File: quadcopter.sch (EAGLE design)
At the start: 67 parts, among them J1 AVR_SPI_PRG_6NS, U1 ATMEGA128RFA1, U2 IMU_LSM9DS1TR, Y1 16MHz

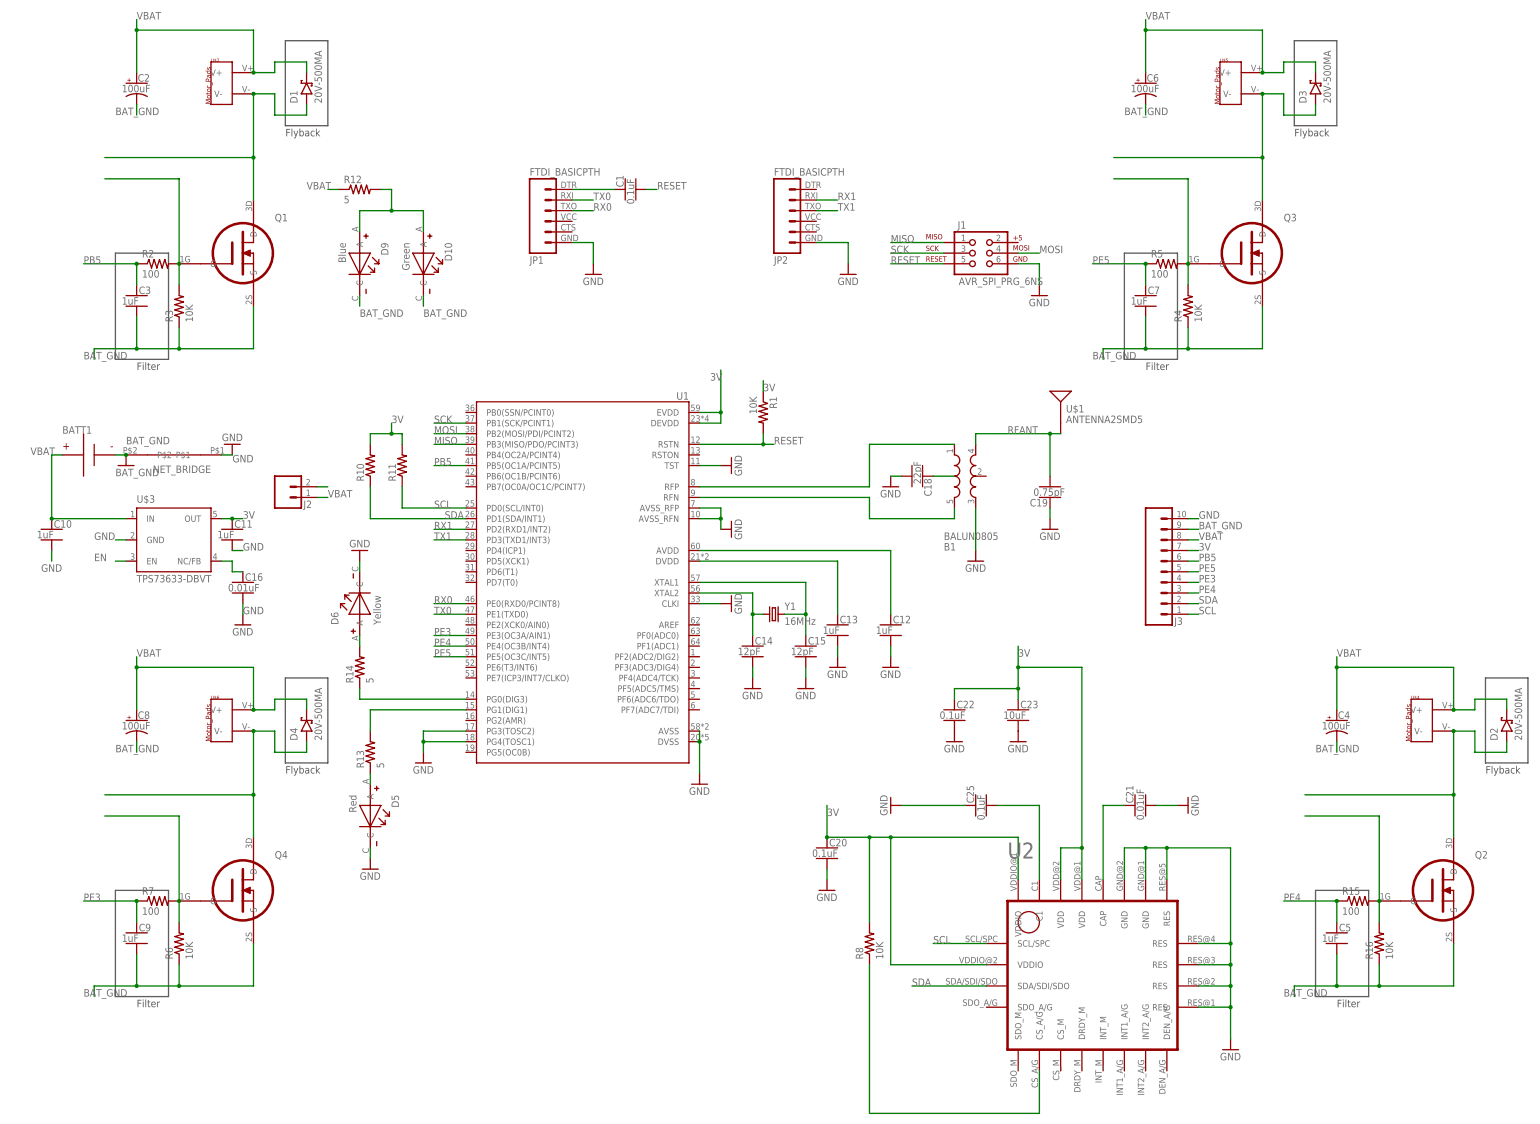
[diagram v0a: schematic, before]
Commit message: Fixed most things from Professor's notes in schematic
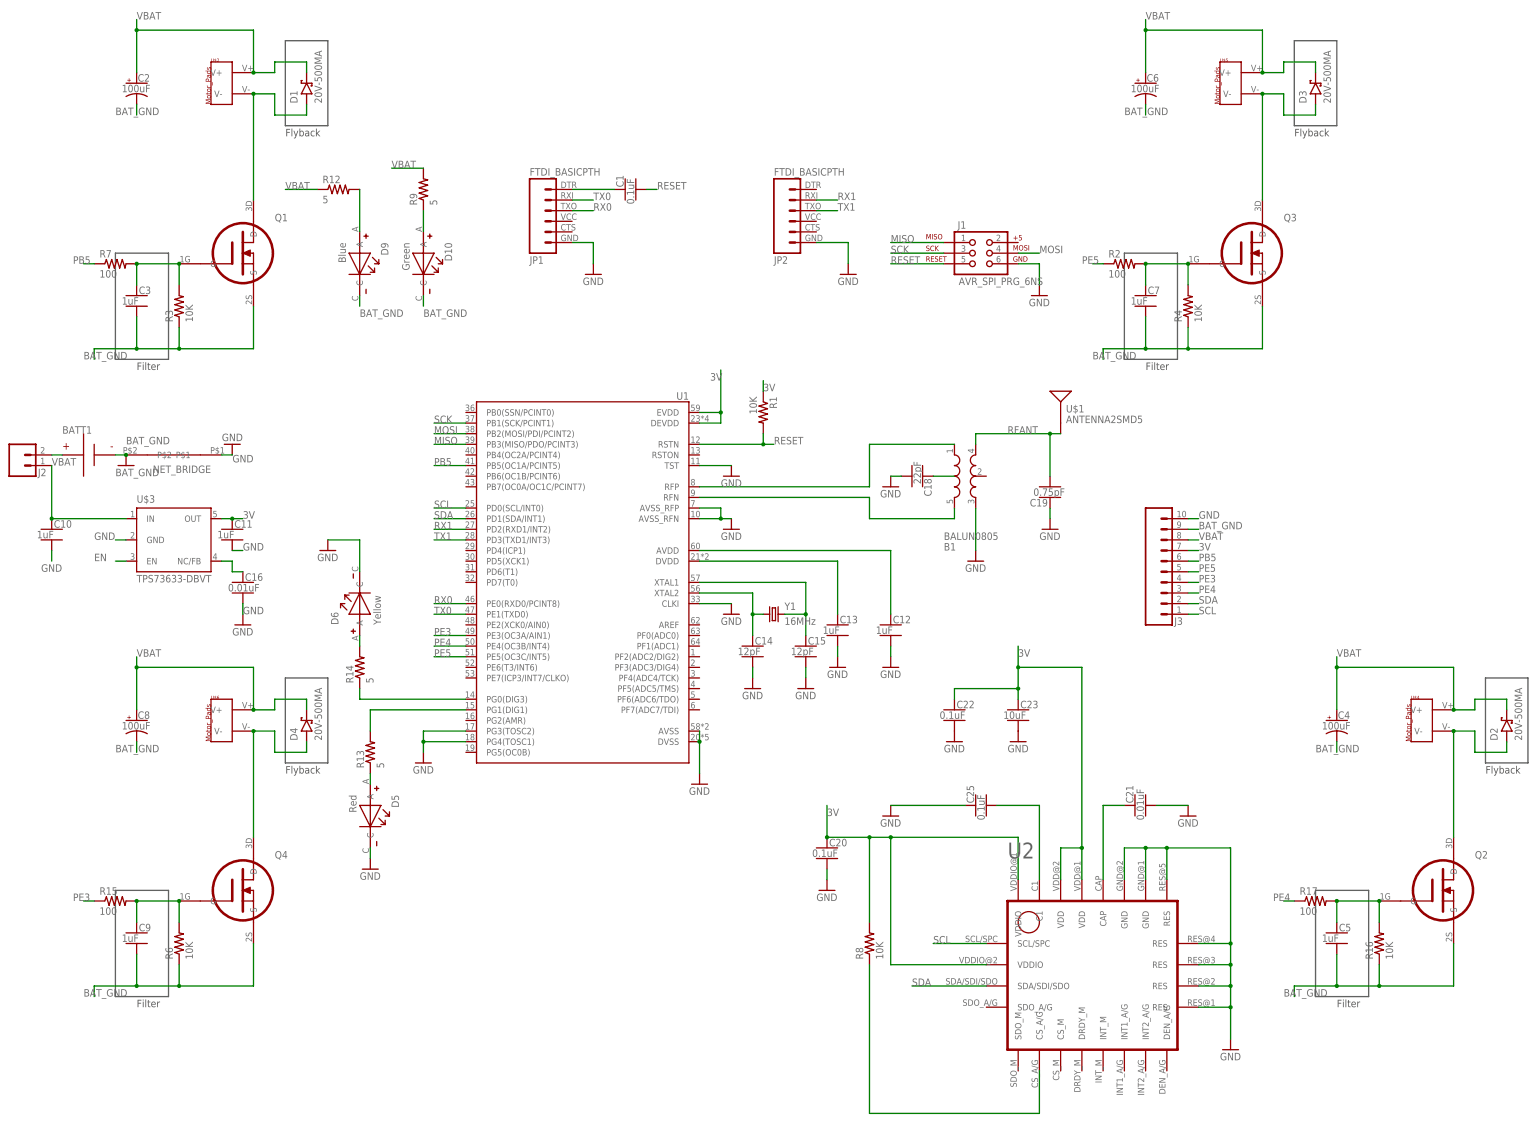
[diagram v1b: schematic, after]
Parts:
- removed R10, R11: (no value), quadparts_prebuilt:RESISTOR_SMD-2012-0805
- removed R5: 100, quadparts_prebuilt:RESISTOR_SMD-2012-0805-100
- added R17: 100, quadparts_prebuilt:RESISTOR_SMD-2012-0805-100
- added R9: 5, quadparts_prebuilt:RESISTOR_SMD-2012-0805
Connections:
- new net N$18: D10.A, R9.1
- new net N$23: BATT1.P, J2.2
- net 3V: no longer R10.2, R11.2
- net FILTERED: now also C7.1, C9.1; no longer Q1.G, Q2.G, R16.2, R3.2, R5.2, R7.2
- net GND: no longer J2.2
- net N$27: no longer D10.A
- net PB5: now also Q1.G, R3.2, R7.1, R7.2; no longer R2.1
- net PE3: now also R15.1; no longer C9.1, R7.1
- net PE4: now also Q2.G, R16.2, R17.1, R17.2; no longer R15.1
- net PE5: now also R2.1; no longer C7.1, R5.1
- net SCL: no longer R11.1
- net SDA: no longer R10.1
- net VBAT: now also R9.2; no longer BATT1.P
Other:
- moved on the sheet: J2, R12, R15, R2, R7

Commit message: stuff
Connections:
- removed net N$16: R8.1, U2.CS_A/G
- net 3V: now also U2.CS_A/G
- net SCL: now also R8.1
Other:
- moved on the sheet: R8
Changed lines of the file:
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@@
 <instance part="C16" gate="G$1" x="-137.16" y="-15.24"/>
 <instance part="GND26" gate="1" x="-137.16" y="-25.4"/>
-<instance part="R8" gate="G$1" x="12.7" y="-101.6" rot="R90"/>
+<instance part="R8" gate="G$1" x="27.94" y="-91.44" rot="R90"/>
 <instance part="R9" gate="G$1" x="-93.98" y="78.74" rot="R90"/>
 <instance part="R17" gate="G$1" x="119.38" y="-91.44"/>
@@
 <pinref part="U2" gate="G$1" pin="VDDIO@1"/>
 <wire x1="48.26" y1="-86.36" x2="48.26" y2="-76.2" width="0.1524" layer="91"/>
-<wire x1="48.26" y1="-76.2" x2="17.78" y2="-76.2" width="0.1524" layer="91"/>
+<wire x1="48.26" y1="-76.2" x2="27.94" y2="-76.2" width="0.1524" layer="91"/>
+<wire x1="27.94" y1="-76.2" x2="17.78" y2="-76.2" width="0.1524" layer="91"/>
 <wire x1="17.78" y1="-76.2" x2="12.7" y2="-76.2" width="0.1524" layer="91"/>
 <wire x1="12.7" y1="-76.2" x2="2.54" y2="-76.2" width="0.1524" layer="91"/>
@@
 <junction x="2.54" y="-76.2"/>
 <pinref part="R8" gate="G$1" pin="2"/>
-<wire x1="12.7" y1="-96.52" x2="12.7" y2="-76.2" width="0.1524" layer="91"/>
+<wire x1="27.94" y1="-86.36" x2="27.94" y2="-76.2" width="0.1524" layer="91"/>
+<junction x="27.94" y="-76.2"/>
+<wire x1="53.34" y1="-142.24" x2="12.7" y2="-142.24" width="0.1524" layer="91"/>
+<pinref part="U2" gate="G$1" pin="CS_A/G"/>
+<wire x1="53.34" y1="-132.08" x2="53.34" y2="-142.24" width="0.1524" layer="91"/>
+<wire x1="12.7" y1="-142.24" x2="12.7" y2="-76.2" width="0.1524" layer="91"/>
 <junction x="12.7" y="-76.2"/>
 </segment>
@@
 <wire x1="40.64" y1="-101.6" x2="27.94" y2="-101.6" width="0.1524" layer="91"/>
 <label x="27.94" y="-101.6" size="1.778" layer="95"/>
+<pinref part="R8" gate="G$1" pin="1"/>
+<wire x1="27.94" y1="-101.6" x2="27.94" y2="-96.52" width="0.1524" layer="91"/>
 </segment>
 </net>
@@
 </segment>
 </net>
-<net name="N$16" class="0">
-<segment>
-<wire x1="53.34" y1="-142.24" x2="12.7" y2="-142.24" width="0.1524" layer="91"/>
-<pinref part="U2" gate="G$1" pin="CS_A/G"/>
-<wire x1="53.34" y1="-132.08" x2="53.34" y2="-142.24" width="0.1524" layer="91"/>
-<pinref part="R8" gate="G$1" pin="1"/>
-<wire x1="12.7" y1="-106.68" x2="12.7" y2="-142.24" width="0.1524" layer="91"/>
-</segment>
-</net>

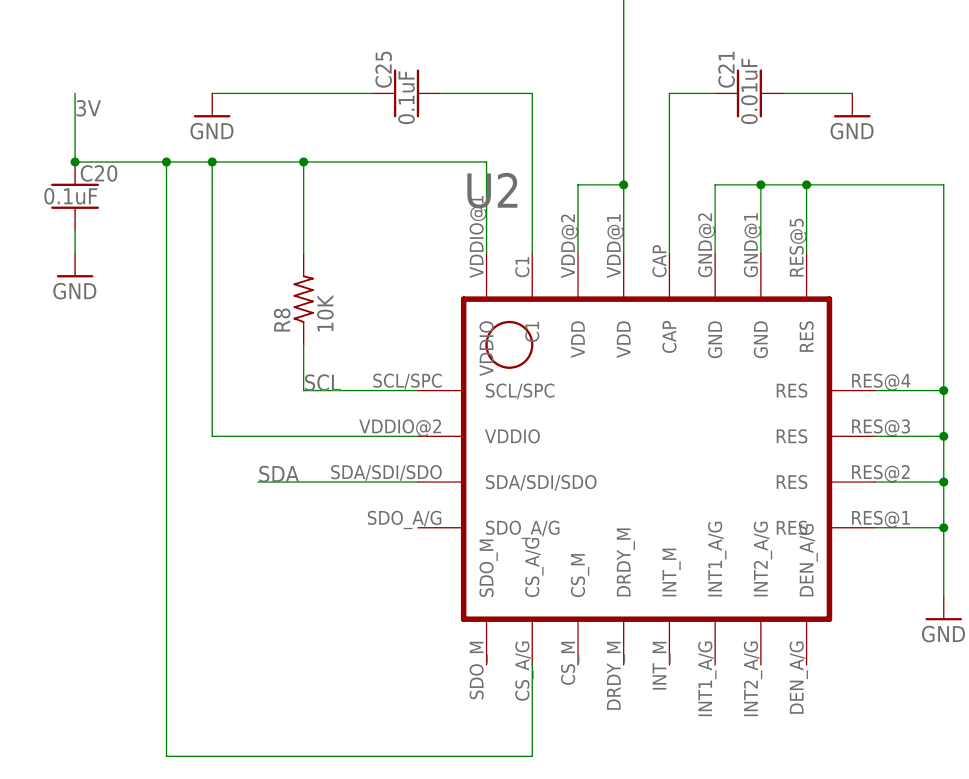
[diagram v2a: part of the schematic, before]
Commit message: IMU is correct now I think?
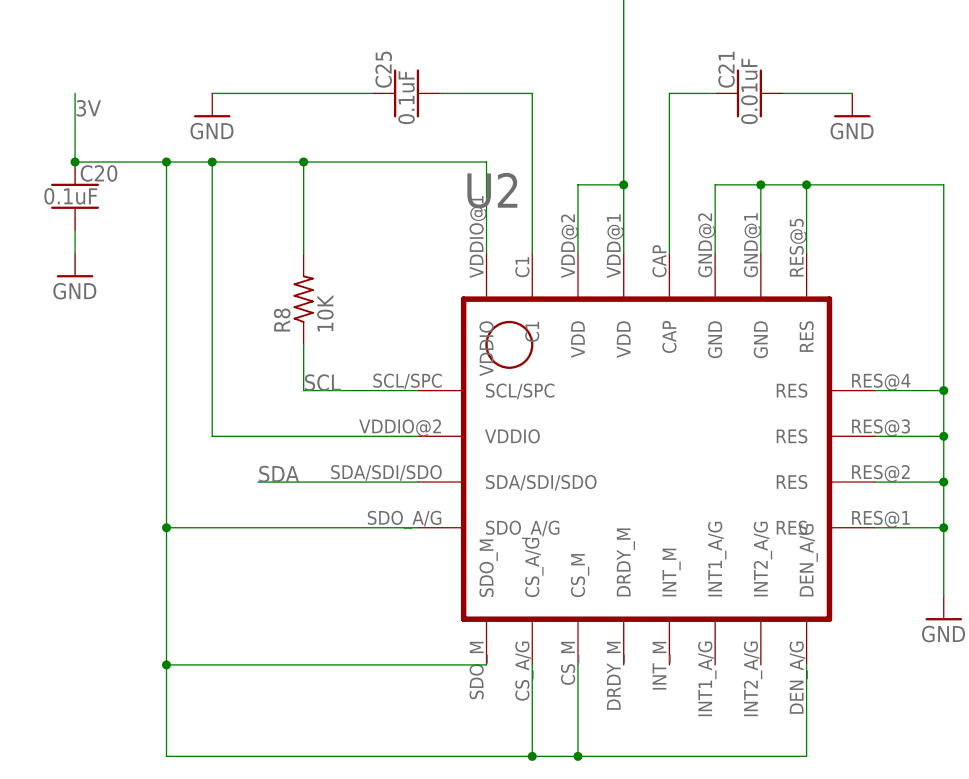
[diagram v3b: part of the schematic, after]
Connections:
- net 3V: now also U2.CS_M, U2.DEN_A/G, U2.SDO_A/G, U2.SDO_M
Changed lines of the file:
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@@
 <pinref part="U2" gate="G$1" pin="CS_A/G"/>
 <wire x1="53.34" y1="-132.08" x2="53.34" y2="-142.24" width="0.1524" layer="91"/>
-<wire x1="12.7" y1="-142.24" x2="12.7" y2="-76.2" width="0.1524" layer="91"/>
+<wire x1="12.7" y1="-142.24" x2="12.7" y2="-132.08" width="0.1524" layer="91"/>
 <junction x="12.7" y="-76.2"/>
+<pinref part="U2" gate="G$1" pin="SDO_A/G"/>
+<wire x1="12.7" y1="-132.08" x2="12.7" y2="-116.84" width="0.1524" layer="91"/>
+<wire x1="12.7" y1="-116.84" x2="12.7" y2="-76.2" width="0.1524" layer="91"/>
+<wire x1="40.64" y1="-116.84" x2="12.7" y2="-116.84" width="0.1524" layer="91"/>
+<junction x="12.7" y="-116.84"/>
+<pinref part="U2" gate="G$1" pin="CS_M"/>
+<wire x1="58.42" y1="-132.08" x2="58.42" y2="-142.24" width="0.1524" layer="91"/>
+<wire x1="58.42" y1="-142.24" x2="53.34" y2="-142.24" width="0.1524" layer="91"/>
+<junction x="53.34" y="-142.24"/>
+<pinref part="U2" gate="G$1" pin="SDO_M"/>
+<wire x1="48.26" y1="-132.08" x2="12.7" y2="-132.08" width="0.1524" layer="91"/>
+<junction x="12.7" y="-132.08"/>
+<pinref part="U2" gate="G$1" pin="DEN_A/G"/>
+<wire x1="83.82" y1="-132.08" x2="83.82" y2="-142.24" width="0.1524" layer="91"/>
+<wire x1="83.82" y1="-142.24" x2="58.42" y2="-142.24" width="0.1524" layer="91"/>
+<junction x="58.42" y="-142.24"/>
 </segment>
 <segment>

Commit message: fixed some schematic stuff
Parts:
- removed R12, R13, R14: 5, quadparts_prebuilt:RESISTOR_SMD-2012-0805
- added R10, R11, R5: 100, quadparts_prebuilt:RESISTOR_SMD-2012-0805-100
- Q1, Q2, Q3, Q4: value (none) -> 2.6A
- R9: value 5 -> 100; device quadparts_prebuilt:RESISTOR_SMD-2012-0805 -> quadparts_prebuilt:RESISTOR_SMD-2012-0805-100
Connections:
- removed net EN: U$3.EN
- removed net FLYBACK: D1.A, D2.A, D3.A, D4.A, Q1.D, Q2.D, Q3.D, Q4.D, U$2.V-, U$4.V-, U$5.V-, U$6.V-
- new net N$16: D1.A, Q1.D, U$2.V-
- new net N$24: D3.A, Q3.D, U$5.V-
- new net N$29: D4.A, Q4.D, U$6.V-
- new net N$30: D2.A, Q2.D, U$4.V-
- new net N$31: C7.1, Q3.G, R2.2, R4.2
- new net N$32: C16.1, U$3.NC/FB
- new net N$33: C3.1, Q1.G, R3.2, R7.2
- new net N$34: C5.1, Q2.G, R16.2, R17.2
- net FILTERED: no longer C7.1, Q3.G, R2.2, R4.2
- net GND: no longer C16.1, U$3.NC/FB
- net N$18: now also R10.2; no longer R9.1
- net N$19: now also R9.2; no longer R13.1
- net N$20: now also R5.2; no longer R14.1
- net N$26: now also R9.1; no longer R13.2
- net N$27: now also R11.1; no longer R12.2
- net N$28: now also R5.1; no longer R14.2
- net PB5: no longer C3.1, Q1.G, R3.2, R7.2
- net PE4: no longer C5.1, Q2.G, R16.2, R17.2
- net VBAT: now also R10.1, R11.2; no longer R12.1, R9.2
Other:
- moved on the sheet: R9

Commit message: Some changes to brd
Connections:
- net GND: now also B1.GND@5; no longer B1.OUT2
- net N$21: now also B1.OUT1; no longer B1.IN
- net N$22: now also B1.OUT2; no longer B1.GND@5
- net N$25: now also B1.GND@2
- net RFANT: now also B1.IN; no longer B1.OUT1
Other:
- moved on the sheet: B1, U$1
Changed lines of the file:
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@@
 <?xml version="1.0" encoding="utf-8"?>
 <!DOCTYPE eagle SYSTEM "eagle.dtd">
-<eagle version="8.1.1">
+<eagle version="8.0.0">
 <drawing>
 <settings>
@@
 <instance part="JP2" gate="G$1" x="-5.08" y="73.66" rot="MR180"/>
 <instance part="J1" gate="G$1" x="38.1" y="63.5"/>
-<instance part="U$1" gate="G$1" x="58.42" y="25.4"/>
+<instance part="U$1" gate="G$1" x="55.88" y="25.4"/>
 <instance part="GND1" gate="1" x="-53.34" y="58.42"/>
 <instance part="C1" gate="G$1" x="-45.72" y="78.74" rot="R90"/>
@@
 <instance part="GND13" gate="1" x="-93.98" y="-58.42"/>
 <instance part="GND14" gate="1" x="-27.94" y="-63.5"/>
-<instance part="B1" gate="G$1" x="35.56" y="12.7"/>
+<instance part="B1" gate="G$1" x="35.56" y="12.7" rot="MR0"/>
 <instance part="C18" gate="G$1" x="25.4" y="10.16" rot="R270"/>
 <instance part="GND15" gate="1" x="17.78" y="7.62"/>
@@
 </segment>
 <segment>
-<pinref part="B1" gate="G$1" pin="OUT2"/>
-<pinref part="GND16" gate="1" pin="GND"/>
-<wire x1="38.1" y1="2.54" x2="38.1" y2="-7.62" width="0.1524" layer="91"/>
-</segment>
-<segment>
 <pinref part="C19" gate="G$1" pin="1"/>
 <wire x1="55.88" y1="2.54" x2="55.88" y2="0" width="0.1524" layer="91"/>
@@
 <wire x1="-116.84" y1="-5.08" x2="-109.22" y2="-5.08" width="0.1524" layer="91"/>
 <wire x1="-109.22" y1="-5.08" x2="-109.22" y2="-12.7" width="0.1524" layer="91"/>
+</segment>
+<segment>
+<pinref part="B1" gate="G$1" pin="GND@5"/>
+<pinref part="GND16" gate="1" pin="GND"/>
+<wire x1="38.1" y1="2.54" x2="38.1" y2="-7.62" width="0.1524" layer="91"/>
 </segment>
 </net>
@@
 <wire x1="-27.94" y1="7.62" x2="12.7" y2="7.62" width="0.1524" layer="91"/>
 <wire x1="12.7" y1="7.62" x2="12.7" y2="17.78" width="0.1524" layer="91"/>
-<pinref part="B1" gate="G$1" pin="IN"/>
+<pinref part="B1" gate="G$1" pin="OUT1"/>
 <wire x1="12.7" y1="17.78" x2="33.02" y2="17.78" width="0.1524" layer="91"/>
 </segment>
@@
 <wire x1="-27.94" y1="5.08" x2="12.7" y2="5.08" width="0.1524" layer="91"/>
 <wire x1="12.7" y1="5.08" x2="12.7" y2="0" width="0.1524" layer="91"/>
-<pinref part="B1" gate="G$1" pin="GND@5"/>
-<wire x1="33.02" y1="0" x2="33.02" y2="2.54" width="0.1524" layer="91"/>
 <wire x1="12.7" y1="0" x2="33.02" y2="0" width="0.1524" layer="91"/>
-</segment>
-</net>
-<net name="N$25" class="0">
-<segment>
-<wire x1="33.02" y1="10.16" x2="27.94" y2="10.16" width="0.1524" layer="91"/>
-<pinref part="C18" gate="G$1" pin="1"/>
+<pinref part="B1" gate="G$1" pin="OUT2"/>
+<wire x1="33.02" y1="2.54" x2="33.02" y2="0" width="0.1524" layer="91"/>
 </segment>
 </net>
 <net name="RFANT" class="1">
 <segment>
-<pinref part="B1" gate="G$1" pin="OUT1"/>
-<wire x1="38.1" y1="17.78" x2="38.1" y2="20.32" width="0.1524" layer="91"/>
-<wire x1="38.1" y1="20.32" x2="55.88" y2="20.32" width="0.1524" layer="91"/>
 <pinref part="U$1" gate="G$1" pin="SIGNAL"/>
-<wire x1="55.88" y1="20.32" x2="58.42" y2="20.32" width="0.1524" layer="91"/>
-<wire x1="55.88" y1="20.32" x2="55.88" y2="10.16" width="0.1524" layer="91"/>
-<junction x="55.88" y="20.32"/>
+<wire x1="55.88" y1="20.32" x2="55.88" y2="17.78" width="0.1524" layer="91"/>
 <pinref part="C19" gate="G$1" pin="2"/>
 <label x="45.72" y="20.32" size="1.778" layer="95"/>
+<pinref part="B1" gate="G$1" pin="IN"/>
+<wire x1="55.88" y1="17.78" x2="55.88" y2="10.16" width="0.1524" layer="91"/>
+<wire x1="38.1" y1="17.78" x2="55.88" y2="17.78" width="0.1524" layer="91"/>
+<junction x="55.88" y="17.78"/>
 </segment>
 </net>
@@
 </segment>
 </net>
+<net name="N$25" class="0">
+<segment>
+<pinref part="C18" gate="G$1" pin="1"/>
+<pinref part="B1" gate="G$1" pin="GND@2"/>
+<wire x1="27.94" y1="10.16" x2="30.48" y2="10.16" width="0.1524" layer="91"/>
+</segment>
+</net>
